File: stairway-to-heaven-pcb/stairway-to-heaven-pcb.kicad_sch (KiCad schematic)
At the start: 2 parts, among them J15 PJ-063AH, U1 MEGA_PRO_EMBED_CH340G_{slash}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

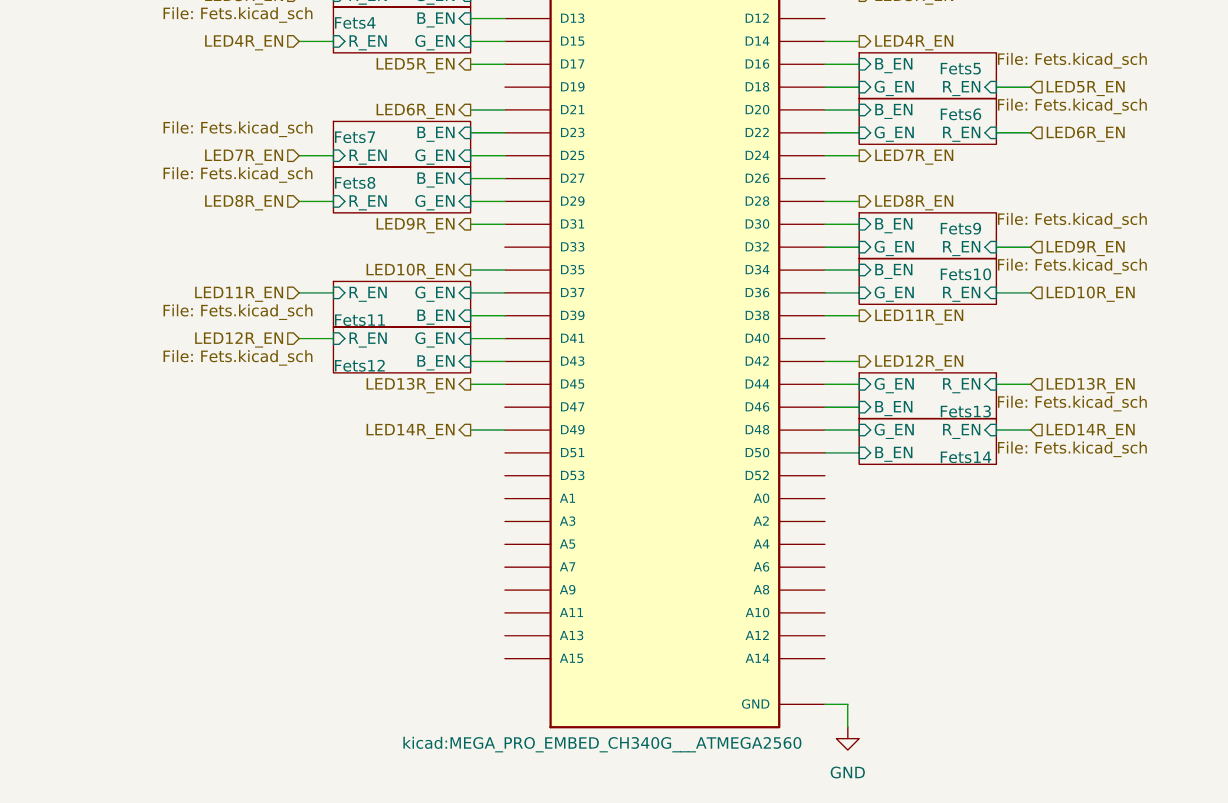
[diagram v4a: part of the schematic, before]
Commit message: replace 5V side, via galore, lots of ground areas checked, rest of the signals places
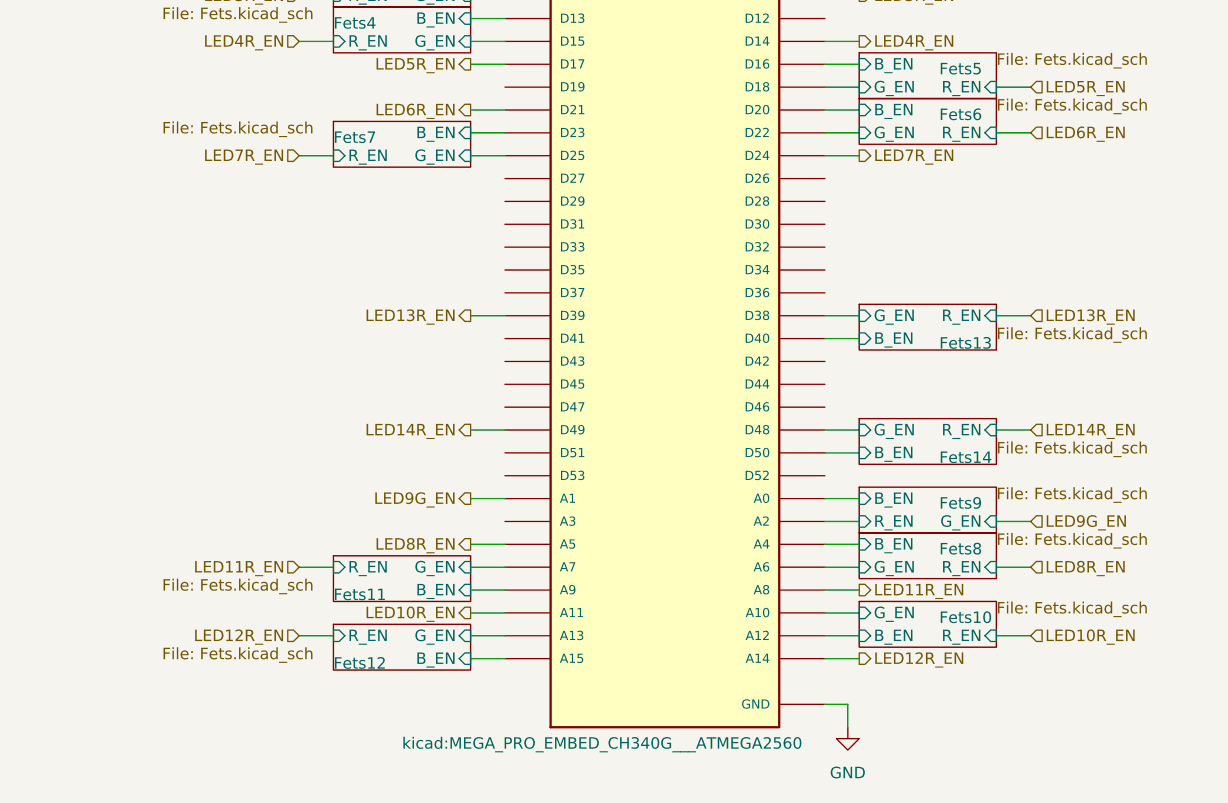
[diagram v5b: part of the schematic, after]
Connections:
- net Fets10/B_EN: now also U1.A12; no longer U1.D34
- net Fets10/G_EN: now also U1.A10; no longer U1.D36
- net Fets11/B_EN: now also U1.A9; no longer U1.D39
- net Fets11/G_EN: now also U1.A7; no longer U1.D37
- net Fets12/B_EN: now also U1.A15; no longer U1.D43
- net Fets12/G_EN: now also U1.A13; no longer U1.D41
- net Fets13/B_EN: now also U1.D40; no longer U1.D46
- net Fets13/G_EN: now also U1.D38; no longer U1.D44
- net Fets8/B_EN: now also U1.A4; no longer U1.D27
- net Fets8/G_EN: now also U1.A6; no longer U1.D29
- net Fets9/B_EN: now also U1.A0; no longer U1.D30
- net LED10R_EN: now also U1.A11; no longer U1.D35
- net LED11R_EN: now also U1.A8; no longer U1.D38
- net LED12R_EN: now also U1.A14; no longer U1.D42
- net LED13R_EN: now also U1.D39; no longer U1.D45
- net LED8R_EN: now also U1.A5; no longer U1.D28
- net LED9G_EN: now reaches U1.A1
- net Fets9/R_EN: now reaches U1.A2
- net Fets9/G_EN: no longer names the net of U1.D32
- net LED9R_EN: no longer names the net of U1.D31

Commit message: Vias galore
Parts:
- added R1, R2, R3: 0R, Resistor_SMD:R_1206_3216Metric, symbol Device:R
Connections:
- net Fets7/B_EN: now also U1.D29; no longer U1.D23
- net Fets7/G_EN: now also U1.D31; no longer U1.D25
- net GND: now also R1.1, R1.2, R2.1, R2.2, R3.1, R3.2
- net LED7R_EN: now also U1.D30; no longer U1.D24

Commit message: vias
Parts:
- added R46: 0R, Resistor_SMD:R_1206_3216Metric, symbol Device:R
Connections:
- net GND: now also R46.1, R46.2
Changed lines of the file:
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@@
   (junction (at 53.34 77.47) (diameter 0) (color 0 0 0 0)
+  )
+  (junction (at 38.1 77.47) (diameter 0) (color 0 0 0 0)
+  )
+  (junction (at 38.1 87.63) (diameter 0) (color 0 0 0 0)
   )
   (junction (at 59.69 87.63) (diameter 0) (color 0 0 0 0)
@@
     (stroke (width 0) (type default) (color 0 0 0 0))
   )
+  (wire (pts (xy 30.48 87.63) (xy 38.1 87.63))
+    (stroke (width 0) (type default) (color 0 0 0 0))
+  )
   (wire (pts (xy 184.15 118.11) (xy 187.96 118.11))
     (stroke (width 0) (type default) (color 0 0 0 0))
@@
     (stroke (width 0) (type default) (color 0 0 0 0))
   )
+  (wire (pts (xy 30.48 86.36) (xy 30.48 87.63))
+    (stroke (width 0) (type default) (color 0 0 0 0))
+  )
   (wire (pts (xy 165.1 138.43) (xy 168.91 138.43))
     (stroke (width 0) (type default) (color 0 0 0 0))
   )
+  (wire (pts (xy 30.48 77.47) (xy 38.1 77.47))
+    (stroke (width 0) (type default) (color 0 0 0 0))
+  )
   (wire (pts (xy 66.04 49.53) (xy 68.58 49.53))
     (stroke (width 0) (type default) (color 0 0 0 0))
@@
   )
   (wire (pts (xy 66.04 52.07) (xy 68.58 52.07))
+    (stroke (width 0) (type default) (color 0 0 0 0))
+  )
+  (wire (pts (xy 30.48 78.74) (xy 30.48 77.47))
     (stroke (width 0) (type default) (color 0 0 0 0))
   )
@@
     (pin "1")
   )
+  (symbol (lib_id "Device:R") (at 30.48 82.55 180) (unit 1)
+    (in_bom yes) (on_board yes) (fields_autoplaced)
+    (property "Reference" "R46" (id 0) (at 33.02 81.2799 0)
+      (effects (font (size 1.27 1.27)) (justify right))
+    )
+    (property "Value" "0R" (id 1) (at 33.02 83.8199 0)
+      (effects (font (size 1.27 1.27)) (justify right))
+    )
+    (property "Footprint" "Resistor_SMD:R_1206_3216Metric" (id 2) (at 32.258 82.55 90)
+      (effects (font (size 1.27 1.27)) hide)
+    )
+    (property "Datasheet" "~" (id 3) (at 30.48 82.55 0)
+      (effects (font (size 1.27 1.27)) hide)
+    )
+    (pin "1")
+    (pin "2")
+  )
   (symbol (lib_id "power:GND") (at 167.64 163.83 0) (unit 1)
     (in_bom yes) (on_board yes) (fields_autoplaced)
@@
       (reference "R45") (unit 1) (value "50k") (footprint "Resistor_SMD:R_0805_2012Metric")
     )
+    (path "/d55bd6d0-3dd4-4415-832b-0acecc2890ca"
+      (reference "R46") (unit 1) (value "0R") (footprint "Resistor_SMD:R_1206_3216Metric")
+    )
     (path "/25cf98c8-de8d-4b21-86b9-2563caa0bbdb"
